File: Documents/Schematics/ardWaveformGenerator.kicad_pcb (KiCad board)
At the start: 2 copper layers, 108 x 52.7 mm, 24 parts, among them J1 Conn_Coaxial, J2 4-pin_I2C_LCD_header, U1 KY-040_Rotary_Encoder, U2 GY-9833_AD9833, U3 3-pole_Power_input_screw_term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, U4 TL071, U5 LM7812_TO220, U6 LM7912_TO220, U7 LM7805_TO220

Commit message: kicad pcb
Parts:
- moved F2 8.26 mm to (47.6, 64.8), turned to 270 degrees
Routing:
- net GND: track 361.8 -> 325.3 mm, vias 4 -> 2
- net Net-(F2-Pad2): track 11.4 -> 23.5 mm
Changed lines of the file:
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@@
   (general
     (thickness 1.6)
-    (drawings 31)
-    (tracks 195)
+    (drawings 28)
+    (tracks 190)
     (zones 0)
     (modules 24)
@@
     (uvia_drill 0.1)
   )
+  (module My_Headers:2-pin_Fuse_header_large (layer F.Cu)
+    (at 47.625 64.77 270)
+    (descr "Through hole straight pin header, 1x02, 2.54mm pitch, single row")
+    (tags "Through hole pin header THT 1x02 2.54mm single row")
+    (fp_text reference F2 (at 0 -2.33 90) (layer F.SilkS)
+      (effects (font (size 1 1) (thickness 0.15)))
+    )
+    (fp_text value Fuse (at 0 4.87 90) (layer F.Fab) hide
+      (effects (font (size 1 1) (thickness 0.15)))
+    )
+    (fp_line (start 3 -1) (end 3 4) (layer F.SilkS) (width 0.15))
+    (fp_line (start 3.5 0) (end 2.5 0) (layer F.SilkS) (width 0.15))
+    (fp_line (start 3.5 3) (end 3.5 0) (layer F.SilkS) (width 0.15))
+    (fp_line (start 2.5 3) (end 3.5 3) (layer F.SilkS) (width 0.15))
+    (fp_line (start 2.5 0) (end 2.5 3) (layer F.SilkS) (width 0.15))
+    (fp_line (start -0.635 -1.27) (end 1.27 -1.27) (layer F.Fab) (width 0.1))
+    (fp_line (start 1.27 -1.27) (end 1.27 3.81) (layer F.Fab) (width 0.1))
+    (fp_line (start 1.27 3.81) (end -1.27 3.81) (layer F.Fab) (width 0.1))
+    (fp_line (start -1.27 3.81) (end -1.27 -0.635) (layer F.Fab) (width 0.1))
+    (fp_line (start -1.27 -0.635) (end -0.635 -1.27) (layer F.Fab) (width 0.1))
+    (fp_line (start -1.33 3.87) (end 1.33 3.87) (layer F.SilkS) (width 0.12))
+    (fp_line (start -1.33 1.27) (end -1.33 3.87) (layer F.SilkS) (width 0.12))
+    (fp_line (start 1.33 1.27) (end 1.33 3.87) (layer F.SilkS) (width 0.12))
+    (fp_line (start -1.33 1.27) (end 1.33 1.27) (layer F.SilkS) (width 0.12))
+    (fp_line (start -1.33 0) (end -1.33 -1.33) (layer F.SilkS) (width 0.12))
+    (fp_line (start -1.33 -1.33) (end 0 -1.33) (layer F.SilkS) (width 0.12))
+    (fp_line (start -1.8 -1.8) (end -1.8 4.35) (layer F.CrtYd) (width 0.05))
+    (fp_line (start -1.8 4.35) (end 1.8 4.35) (layer F.CrtYd) (width 0.05))
+    (fp_line (start 1.8 4.35) (end 1.8 -1.8) (layer F.CrtYd) (width 0.05))
+    (fp_line (start 1.8 -1.8) (end -1.8 -1.8) (layer F.CrtYd) (width 0.05))
+    (pad 1 thru_hole rect (at 0 0 270) (size 3.048 2.032) (drill 1) (layers *.Cu *.Mask)
+      (net 5 GND))
+    (pad 2 thru_hole oval (at 0 2.54 270) (size 3.048 2.032) (drill 1) (layers *.Cu *.Mask)
+      (net 37 "Net-(F2-Pad2)"))
+    (model ${KISYS3DMOD}/Connector_PinHeader_2.54mm.3dshapes/PinHeader_1x02_P2.54mm_Vertical.wrl
+      (at (xyz 0 0 0))
+      (scale (xyz 1 1 1))
+      (rotate (xyz 0 0 0))
+    )
+  )
   (module My_Misc:DIP-8_W7.62mm_large (layer F.Cu)
     (at 51.435 106.68 180)
@@
     (pad 2 thru_hole oval (at 0 2.54 180) (size 3.048 2.032) (drill 1) (layers *.Cu *.Mask)
       (net 5 GND))
-    (model ${KISYS3DMOD}/Connector_PinHeader_2.54mm.3dshapes/PinHeader_1x02_P2.54mm_Vertical.wrl
-      (at (xyz 0 0 0))
-      (scale (xyz 1 1 1))
-      (rotate (xyz 0 0 0))
-    )
-  )
-  (module My_Headers:2-pin_Fuse_header_large (layer F.Cu)
-    (at 47.625 73.025)
-    (descr "Through hole straight pin header, 1x02, 2.54mm pitch, single row")
-    (tags "Through hole pin header THT 1x02 2.54mm single row")
-    (fp_text reference F2 (at 0 -2.33) (layer F.SilkS)
-      (effects (font (size 1 1) (thickness 0.15)))
-    )
-    (fp_text value Fuse (at 0 4.87) (layer F.Fab) hide
-      (effects (font (size 1 1) (thickness 0.15)))
-    )
-    (fp_line (start 3 -1) (end 3 4) (layer F.SilkS) (width 0.15))
-    (fp_line (start 3.5 0) (end 2.5 0) (layer F.SilkS) (width 0.15))
-    (fp_line (start 3.5 3) (end 3.5 0) (layer F.SilkS) (width 0.15))
-    (fp_line (start 2.5 3) (end 3.5 3) (layer F.SilkS) (width 0.15))
-    (fp_line (start 2.5 0) (end 2.5 3) (layer F.SilkS) (width 0.15))
-    (fp_line (start -0.635 -1.27) (end 1.27 -1.27) (layer F.Fab) (width 0.1))
-    (fp_line (start 1.27 -1.27) (end 1.27 3.81) (layer F.Fab) (width 0.1))
-    (fp_line (start 1.27 3.81) (end -1.27 3.81) (layer F.Fab) (width 0.1))
-    (fp_line (start -1.27 3.81) (end -1.27 -0.635) (layer F.Fab) (width 0.1))
-    (fp_line (start -1.27 -0.635) (end -0.635 -1.27) (layer F.Fab) (width 0.1))
-    (fp_line (start -1.33 3.87) (end 1.33 3.87) (layer F.SilkS) (width 0.12))
-    (fp_line (start -1.33 1.27) (end -1.33 3.87) (layer F.SilkS) (width 0.12))
-    (fp_line (start 1.33 1.27) (end 1.33 3.87) (layer F.SilkS) (width 0.12))
-    (fp_line (start -1.33 1.27) (end 1.33 1.27) (layer F.SilkS) (width 0.12))
-    (fp_line (start -1.33 0) (end -1.33 -1.33) (layer F.SilkS) (width 0.12))
-    (fp_line (start -1.33 -1.33) (end 0 -1.33) (layer F.SilkS) (width 0.12))
-    (fp_line (start -1.8 -1.8) (end -1.8 4.35) (layer F.CrtYd) (width 0.05))
-    (fp_line (start -1.8 4.35) (end 1.8 4.35) (layer F.CrtYd) (width 0.05))
-    (fp_line (start 1.8 4.35) (end 1.8 -1.8) (layer F.CrtYd) (width 0.05))
-    (fp_line (start 1.8 -1.8) (end -1.8 -1.8) (layer F.CrtYd) (width 0.05))
-    (pad 1 thru_hole rect (at 0 0) (size 3.048 2.032) (drill 1) (layers *.Cu *.Mask)
-      (net 5 GND))
-    (pad 2 thru_hole oval (at 0 2.54) (size 3.048 2.032) (drill 1) (layers *.Cu *.Mask)
-      (net 37 "Net-(F2-Pad2)"))
     (model ${KISYS3DMOD}/Connector_PinHeader_2.54mm.3dshapes/PinHeader_1x02_P2.54mm_Vertical.wrl
       (at (xyz 0 0 0))
@@
     )
   )
-  (gr_text GND (at 43.815 64.77) (layer B.Cu)
-    (effects (font (size 0.889 0.889) (thickness 0.2032)) (justify mirror))
-  )
   (gr_text GND (at 56.515 111.76) (layer B.Cu)
     (effects (font (size 0.889 0.889) (thickness 0.2032)) (justify mirror))
@@
   )
   (gr_text +5V (at 132.08 76.2) (layer B.Cu)
-    (effects (font (size 0.889 0.889) (thickness 0.2032)) (justify mirror))
-  )
-  (gr_text GND (at 40.005 73.025) (layer B.Cu)
     (effects (font (size 0.889 0.889) (thickness 0.2032)) (justify mirror))
   )
@@
   (gr_text -12V (at 108.585 63.5) (layer F.SilkS)
     (effects (font (size 1 1) (thickness 0.15)))
-  )
-  (gr_text GND (at 108.585 73.025) (layer F.SilkS)
-    (effects (font (size 1.27 1.27) (thickness 0.15)))
   )
   (segment (start 119.12599 96.26601) (end 119.38 96.012) (width 0.508) (layer B.Cu) (net 1))
@@
   (segment (start 65.028 99.57) (end 60.830989 103.767011) (width 0.508) (layer B.Cu) (net 4))
   (segment (start 116.84 111.252) (end 116.84 109.22) (width 0.508) (layer B.Cu) (net 4))
-  (segment (start 47.625 73.025) (end 43.18 73.025) (width 1.27) (layer B.Cu) (net 5))
-  (segment (start 43.18 73.025) (end 43.18 73.025) (width 1.27) (layer B.Cu) (net 5))
-  (via (at 43.18 73.025) (size 2.54) (drill 0.762) (layers F.Cu B.Cu) (net 5))
   (segment (start 66.04 70.485) (end 66.04 77.47) (width 1.27) (layer B.Cu) (net 5))
   (segment (start 68.58 80.01) (end 75.311 80.01) (width 1.27) (layer B.Cu) (net 5))
@@
   (segment (start 52.22201 113.51299) (end 51.559979 113.51299) (width 0.508) (layer B.Cu) (net 5))
   (segment (start 56.515 109.22) (end 52.22201 113.51299) (width 0.508) (layer B.Cu) (net 5))
-  (via (at 43.815 67.31) (size 2.54) (drill 0.762) (layers F.Cu B.Cu) (net 5))
-  (segment (start 42.018949 67.31) (end 43.815 67.31) (width 0.508) (layer B.Cu) (net 5))
-  (segment (start 33.934398 67.31) (end 42.018949 67.31) (width 0.508) (layer B.Cu) (net 5))
-  (segment (start 33.400999 88.137999) (end 33.400999 67.843399) (width 0.508) (layer B.Cu) (net 5))
-  (segment (start 33.400999 67.843399) (end 33.934398 67.31) (width 0.508) (layer B.Cu) (net 5))
-  (segment (start 34.163 88.9) (end 33.400999 88.137999) (width 0.508) (layer B.Cu) (net 5))
   (segment (start 36.195 88.9) (end 34.163 88.9) (width 0.508) (layer B.Cu) (net 5))
   (segment (start 62.771559 111.508001) (end 113.281999 111.508001) (width 0.508) (layer B.Cu) (net 6))
@@
   (segment (start 36.195 80.485) (end 51.595 80.485) (width 1.27) (layer B.Cu) (net 36))
   (segment (start 51.595 80.485) (end 55.88 76.2) (width 1.27) (layer B.Cu) (net 36))
-  (segment (start 36.195 75.485) (end 47.545 75.485) (width 1.27) (layer B.Cu) (net 37))
+  (segment (start 33.019999 75.18368) (end 33.019999 67.538599) (width 1.27) (layer B.Cu) (net 37))
+  (segment (start 36.195 75.485) (end 33.321319 75.485) (width 1.27) (layer B.Cu) (net 37))
+  (segment (start 33.019999 67.538599) (end 35.788598 64.77) (width 1.27) (layer B.Cu) (net 37))
+  (segment (start 33.321319 75.485) (end 33.019999 75.18368) (width 1.27) (layer B.Cu) (net 37))
+  (segment (start 35.788598 64.77) (end 44.45 64.77) (width 1.27) (layer B.Cu) (net 37))
   (segment (start 43.815 101.6) (end 36.195 101.6) (width 0.508) (layer B.Cu) (net 38))
   (segment (start 33.90899 101.34599) (end 33.90899 94.36101) (width 0.508) (layer B.Cu) (net 38))

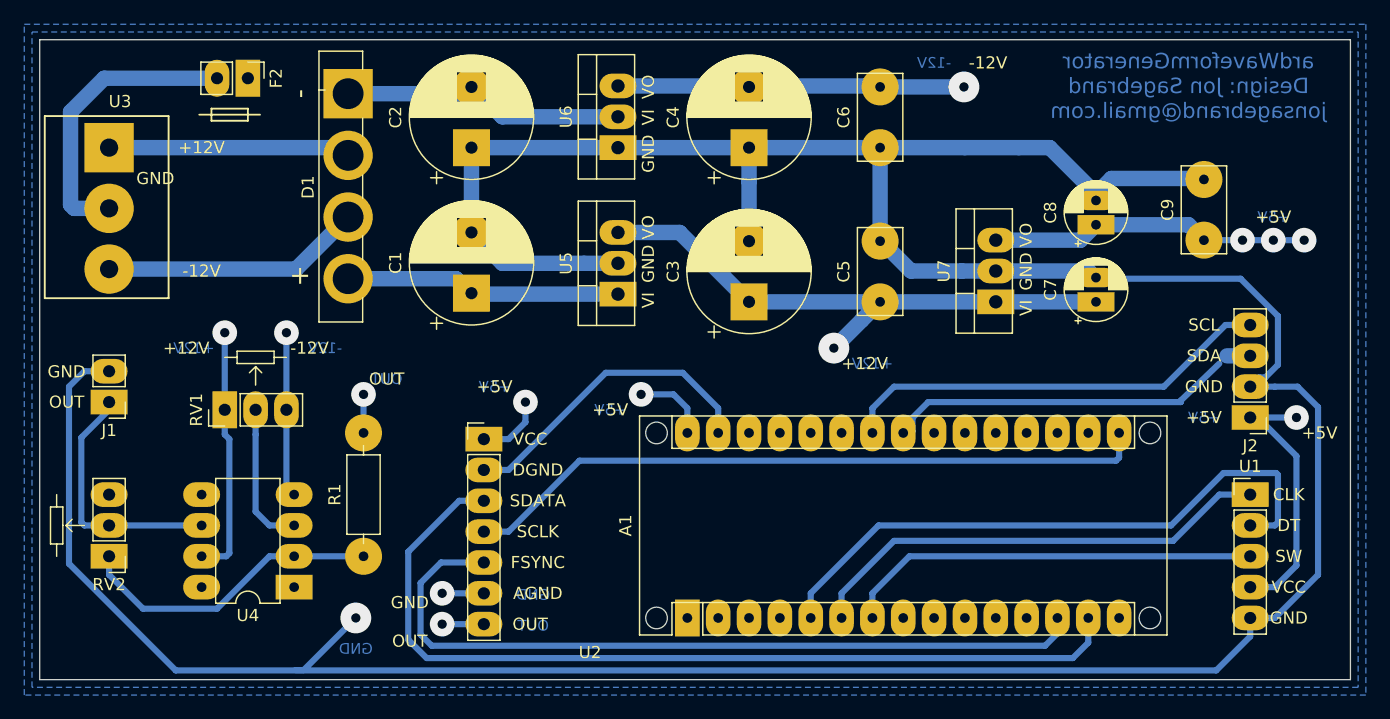
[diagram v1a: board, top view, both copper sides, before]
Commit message: new pcb layout
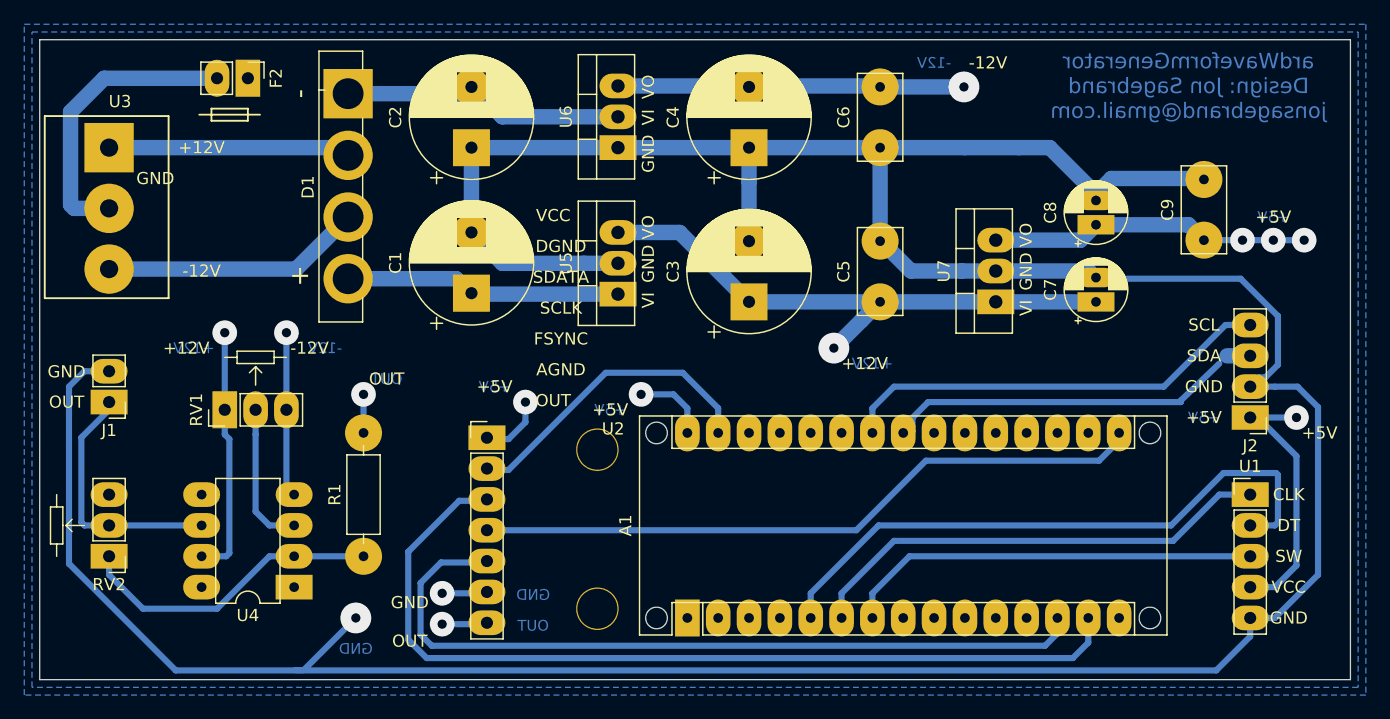
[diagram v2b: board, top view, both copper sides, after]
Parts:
- moved U2 18.5 mm to (67.3, 92.7)
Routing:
- net Net-(A1-Pad16): track 56.9 -> 55.1 mm
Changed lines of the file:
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@@
     (thickness 1.6)
     (drawings 28)
-    (tracks 190)
+    (tracks 189)
     (zones 0)
     (modules 24)
@@
     (uvia_drill 0.1)
   )
+  (module My_Parts:GY-9833_AD9833_larger (layer F.Cu)
+    (at 67.31 92.71 180)
+    (descr "Through hole straight pin header, 1x07, 2.54mm pitch, single row")
+    (tags "Through hole pin header THT 1x07 2.54mm single row")
+    (fp_text reference U2 (at -10.4 -0.935) (layer F.SilkS)
+      (effects (font (size 1 1) (thickness 0.15)))
+    )
+    (fp_text value GY-9833_AD9833 (at -11 9.2 90) (layer F.Fab) hide
+      (effects (font (size 1 1) (thickness 0.15)))
+    )
+    (fp_line (start -10.85 -18.4) (end 1.65 -18.4) (layer F.CrtYd) (width 0.12))
+    (fp_line (start -10.85 0) (end -10.85 -18.4) (layer F.CrtYd) (width 0.12))
+    (fp_line (start 1.65 0) (end -10.85 0) (layer F.CrtYd) (width 0.12))
+    (fp_line (start 1.65 -18.3) (end 1.65 0) (layer F.CrtYd) (width 0.12))
+    (fp_text user OUT (at -5.465 1.395) (layer F.SilkS)
+      (effects (font (size 1 1) (thickness 0.15)))
+    )
+    (fp_text user AGND (at -6.1 3.935) (layer F.SilkS)
+      (effects (font (size 1 1) (thickness 0.15)))
+    )
+    (fp_text user FSYNC (at -6.1 6.475) (layer F.SilkS)
+      (effects (font (size 1 1) (thickness 0.15)))
+    )
+    (fp_text user SCLK (at -6.1 9.015) (layer F.SilkS)
+      (effects (font (size 1 1) (thickness 0.15)))
+    )
+    (fp_text user SDATA (at -6.1 11.555) (layer F.SilkS)
+      (effects (font (size 1 1) (thickness 0.15)))
+    )
+    (fp_text user DGND (at -6.1 14.095) (layer F.SilkS)
+      (effects (font (size 1 1) (thickness 0.15)))
+    )
+    (fp_text user VCC (at -5.465 16.635) (layer F.SilkS)
+      (effects (font (size 1 1) (thickness 0.15)))
+    )
+    (fp_text user %R (at -1.655 9.015 270) (layer F.Fab)
+      (effects (font (size 1 1) (thickness 0.15)))
+    )
+    (fp_line (start 1.325 -0.335) (end -0.005 -0.335) (layer F.SilkS) (width 0.12))
+    (fp_line (start 1.325 -1.665) (end 1.325 -0.335) (layer F.SilkS) (width 0.12))
+    (fp_line (start 1.325 -2.935) (end -1.335 -2.935) (layer F.SilkS) (width 0.12))
+    (fp_line (start -1.335 -2.935) (end -1.335 -18.235) (layer F.SilkS) (width 0.12))
+    (fp_line (start 1.325 -2.935) (end 1.325 -18.235) (layer F.SilkS) (width 0.12))
+    (fp_line (start 1.325 -18.235) (end -1.335 -18.235) (layer F.SilkS) (width 0.12))
+    (fp_line (start 1.265 -1.03) (end 0.63 -0.395) (layer F.Fab) (width 0.1))
+    (fp_line (start 1.265 -18.175) (end 1.265 -1.03) (layer F.Fab) (width 0.1))
+    (fp_line (start -1.275 -18.175) (end 1.265 -18.175) (layer F.Fab) (width 0.1))
+    (fp_line (start -1.275 -0.395) (end -1.275 -18.175) (layer F.Fab) (width 0.1))
+    (fp_line (start 0.63 -0.395) (end -1.275 -0.395) (layer F.Fab) (width 0.1))
+    (pad "" thru_hole circle (at -9.1 -2.65 180) (size 3.5 3.5) (drill 3.3) (layers *.Cu *.Mask))
+    (pad "" thru_hole circle (at -9.1 -15.75 180) (size 3.5 3.5) (drill 3.3) (layers *.Cu *.Mask))
+    (pad 7 thru_hole oval (at -0.005 -16.905) (size 3.048 2.032) (drill 1) (layers *.Cu *.Mask)
+      (net 39 "Net-(R1-Pad2)"))
+    (pad 6 thru_hole oval (at -0.005 -14.365) (size 3.048 2.032) (drill 1) (layers *.Cu *.Mask)
+      (net 5 GND))
+    (pad 5 thru_hole oval (at -0.005 -11.825) (size 3.048 2.032) (drill 1) (layers *.Cu *.Mask)
+      (net 6 "Net-(A1-Pad13)"))
+    (pad 4 thru_hole oval (at -0.005 -9.285) (size 3.048 2.032) (drill 1) (layers *.Cu *.Mask)
+      (net 1 "Net-(A1-Pad16)"))
+    (pad 3 thru_hole oval (at -0.005 -6.745) (size 3.048 2.032) (drill 1) (layers *.Cu *.Mask)
+      (net 4 "Net-(A1-Pad14)"))
+    (pad 2 thru_hole oval (at -0.005 -4.205) (size 3.048 2.032) (drill 1) (layers *.Cu *.Mask)
+      (net 5 GND))
+    (pad 1 thru_hole rect (at -0.005 -1.665) (size 3.048 2.032) (drill 1) (layers *.Cu *.Mask)
+      (net 3 +5V))
+    (model ${KISYS3DMOD}/Connector_PinHeader_2.54mm.3dshapes/PinHeader_1x07_P2.54mm_Vertical.wrl
+      (at (xyz 0 0 0))
+      (scale (xyz 1 1 1))
+      (rotate (xyz 0 0 0))
+    )
+  )
   (module My_Headers:2-pin_Fuse_header_large (layer F.Cu)
     (at 47.625 64.77 270)
@@
       (net 45 "Net-(U4-Pad1)"))
     (model ${KISYS3DMOD}/Package_DIP.3dshapes/DIP-8_W7.62mm.wrl
-      (at (xyz 0 0 0))
-      (scale (xyz 1 1 1))
-      (rotate (xyz 0 0 0))
-    )
-  )
-  (module My_Parts:GY-9833_AD9833_larger (layer F.Cu)
-    (at 65.405 111.125 180)
-    (descr "Through hole straight pin header, 1x07, 2.54mm pitch, single row")
-    (tags "Through hole pin header THT 1x07 2.54mm single row")
-    (fp_text reference U2 (at -10.4 -0.935) (layer F.SilkS)
-      (effects (font (size 1 1) (thickness 0.15)))
-    )
-    (fp_text value GY-9833_AD9833 (at -11 9.2 90) (layer F.Fab) hide
-      (effects (font (size 1 1) (thickness 0.15)))
-    )
-    (fp_line (start -12.5 -0.1) (end 0 -0.1) (layer F.CrtYd) (width 0.12))
-    (fp_line (start -12.5 18.3) (end -12.5 -0.1) (layer F.CrtYd) (width 0.12))
-    (fp_line (start 0 18.3) (end -12.5 18.3) (layer F.CrtYd) (width 0.12))
-    (fp_line (start 0 0) (end 0 18.3) (layer F.CrtYd) (width 0.12))
-    (fp_text user OUT (at -5.465 1.395) (layer F.SilkS)
-      (effects (font (size 1 1) (thickness 0.15)))
-    )
-    (fp_text user AGND (at -6.1 3.935) (layer F.SilkS)
-      (effects (font (size 1 1) (thickness 0.15)))
-    )
-    (fp_text user FSYNC (at -6.1 6.475) (layer F.SilkS)
-      (effects (font (size 1 1) (thickness 0.15)))
-    )
-    (fp_text user SCLK (at -6.1 9.015) (layer F.SilkS)
-      (effects (font (size 1 1) (thickness 0.15)))
-    )
-    (fp_text user SDATA (at -6.1 11.555) (layer F.SilkS)
-      (effects (font (size 1 1) (thickness 0.15)))
-    )
-    (fp_text user DGND (at -6.1 14.095) (layer F.SilkS)
-      (effects (font (size 1 1) (thickness 0.15)))
-    )
-    (fp_text user VCC (at -5.465 16.635) (layer F.SilkS)
-      (effects (font (size 1 1) (thickness 0.15)))
-    )
-    (fp_text user %R (at -1.655 9.015 270) (layer F.Fab)
-      (effects (font (size 1 1) (thickness 0.15)))
-    )
-    (fp_line (start -0.325 17.965) (end -1.655 17.965) (layer F.SilkS) (width 0.12))
-    (fp_line (start -0.325 16.635) (end -0.325 17.965) (layer F.SilkS) (width 0.12))
-    (fp_line (start -0.325 15.365) (end -2.985 15.365) (layer F.SilkS) (width 0.12))
-    (fp_line (start -2.985 15.365) (end -2.985 0.065) (layer F.SilkS) (width 0.12))
-    (fp_line (start -0.325 15.365) (end -0.325 0.065) (layer F.SilkS) (width 0.12))
-    (fp_line (start -0.325 0.065) (end -2.985 0.065) (layer F.SilkS) (width 0.12))
-    (fp_line (start -0.385 17.27) (end -1.02 17.905) (layer F.Fab) (width 0.1))
-    (fp_line (start -0.385 0.125) (end -0.385 17.27) (layer F.Fab) (width 0.1))
-    (fp_line (start -2.925 0.125) (end -0.385 0.125) (layer F.Fab) (width 0.1))
-    (fp_line (start -2.925 17.905) (end -2.925 0.125) (layer F.Fab) (width 0.1))
-    (fp_line (start -1.02 17.905) (end -2.925 17.905) (layer F.Fab) (width 0.1))
-    (pad 7 thru_hole oval (at -1.655 1.395) (size 3.048 2.032) (drill 1) (layers *.Cu *.Mask)
-      (net 39 "Net-(R1-Pad2)"))
-    (pad 6 thru_hole oval (at -1.655 3.935) (size 3.048 2.032) (drill 1) (layers *.Cu *.Mask)
-      (net 5 GND))
-    (pad 5 thru_hole oval (at -1.655 6.475) (size 3.048 2.032) (drill 1) (layers *.Cu *.Mask)
-      (net 6 "Net-(A1-Pad13)"))
-    (pad 4 thru_hole oval (at -1.655 9.015) (size 3.048 2.032) (drill 1) (layers *.Cu *.Mask)
-      (net 1 "Net-(A1-Pad16)"))
-    (pad 3 thru_hole oval (at -1.655 11.555) (size 3.048 2.032) (drill 1) (layers *.Cu *.Mask)
-      (net 4 "Net-(A1-Pad14)"))
-    (pad 2 thru_hole oval (at -1.655 14.095) (size 3.048 2.032) (drill 1) (layers *.Cu *.Mask)
-      (net 5 GND))
-    (pad 1 thru_hole rect (at -1.655 16.635) (size 3.048 2.032) (drill 1) (layers *.Cu *.Mask)
-      (net 3 +5V))
-    (model ${KISYS3DMOD}/Connector_PinHeader_2.54mm.3dshapes/PinHeader_1x07_P2.54mm_Vertical.wrl
       (at (xyz 0 0 0))
       (scale (xyz 1 1 1))
@@
     (effects (font (size 1 1) (thickness 0.15)))
   )
-  (segment (start 119.12599 96.26601) (end 119.38 96.012) (width 0.508) (layer B.Cu) (net 1))
-  (segment (start 74.93599 96.26601) (end 119.12599 96.26601) (width 0.508) (layer B.Cu) (net 1))
-  (segment (start 67.06 102.11) (end 69.092 102.11) (width 0.508) (layer B.Cu) (net 1))
-  (segment (start 69.092 102.11) (end 74.93599 96.26601) (width 0.508) (layer B.Cu) (net 1))
-  (segment (start 119.38 96.012) (end 119.38 93.98) (width 0.508) (layer B.Cu) (net 1))
+  (segment (start 103.465136 96.26601) (end 117.72899 96.26601) (width 0.508) (layer B.Cu) (net 1))
+  (segment (start 67.315 101.995) (end 97.736146 101.995) (width 0.508) (layer B.Cu) (net 1))
+  (segment (start 97.736146 101.995) (end 103.465136 96.26601) (width 0.508) (layer B.Cu) (net 1))
+  (segment (start 117.72899 96.26601) (end 119.38 94.615) (width 0.508) (layer B.Cu) (net 1))
   (segment (start 109.22 78.105) (end 116.205 78.105) (width 1.27) (layer B.Cu) (net 3))
   (segment (start 116.205 78.105) (end 117.475 76.835) (width 1.27) (layer B.Cu) (net 3))
